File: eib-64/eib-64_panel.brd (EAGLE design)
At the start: 76.6 x 77.2 mm, 400 parts, among them J1 DF40-REC, J10 DF40-REC, J11 DF40-REC, J12 DF40-REC, J13 DF40-REC, J14 DF40-REC, J15 DF40-REC, J16 DF40-REC, J2 DF40-REC, J3 DF40-REC, J4 DF40-REC, J5 DF40-REC, J6 DF40-REC, J7 DF40-REC, J8 DF40-REC, J9 DF40-REC

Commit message: Updates to eib-64 for latest shuttle drives
- Decreased outer diameter
- Removed flat spots because they are not required anymore (headstage
retention clips were removed from drive body design)
- Remade panel and added labelled fiducial marks as per Filipe's
requirments
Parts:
- removed GND: LRG_GP, jonnew:GOLDPIN_0.5ID_0.7OD
- added E$1, E$2, E$4: (no value), fiducial:FIDUCIAL
- added GND31: LRG_GP, jonnew:GOLDPIN_0.5ID_0.7OD
- moved GND30 74.9 mm to (81.0, 97.6)
- moved GND28 72.5 mm to (61.0, 97.6)
- moved GND26 70.4 mm to (41.0, 97.6)
- moved GND24 68.6 mm to (21.0, 97.6)
- moved ESTIM15 64.1 mm to (87.4, 94.7)
- moved AN15 64.1 mm to (75.0, 95.4)
- moved CAT31 64.1 mm to (75.6, 94.7)
- moved J16 64.1 mm to (81.0, 92.0)
- moved REF15 64.1 mm to (86.5, 94.7)
- moved TET240 64.1 mm to (81.0, 91.0)
- moved TET241 64.1 mm to (81.0, 91.0)
- moved TET242 64.1 mm to (81.0, 91.0)
- moved TET243 64.1 mm to (81.0, 91.0)
- moved TET244 64.1 mm to (81.0, 91.0)
- moved TET245 64.1 mm to (81.0, 91.0)
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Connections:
- net GND: now also GND31.P$1; no longer GND.P$1
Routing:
- net GND: track 0.00 -> 40.6 mm, vias 240 -> 320
- net CAT7: track 6.44 -> 5.35 mm
- net CAT3: track 6.44 -> 5.35 mm
- net CAT19: track 6.44 -> 5.35 mm
- net CAT23: track 6.44 -> 5.35 mm
- net CAT15: track 6.44 -> 5.35 mm
- net CAT1: track 6.44 -> 5.35 mm
- net CAT11: track 6.44 -> 5.35 mm
- net CAT5: track 6.44 -> 5.35 mm
- net CAT17: track 6.44 -> 5.35 mm
- net CAT9: track 6.44 -> 5.35 mm
- net CAT31: track 6.44 -> 5.35 mm
- net CAT27: track 6.44 -> 5.35 mm
- net CAT21: track 6.44 -> 5.35 mm
- net CAT13: track 6.44 -> 5.35 mm
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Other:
- board size 76.6 x 77.2 mm -> 102 x 113 mm
- board text added: "(6, 11)"
- board text added: "(92, 97)"
- board text added: "(95, 20)"
- board text added: "CERN OHL v1.2 JPN, MWL@MIT 2019"
- board text added: "EIB-64 Rev. 1.2"
- board text added: "EIB-64 r1.2 JPN '19 OHL v1.2"
- board text added: "r1.2"
- board text removed: "EIB-64 JPN '17 OHL v1.2"
- board text removed: "EIB-64 r1.1"
- board text removed: "V-CUT"

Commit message: Address Filipe's issues with eib-64 prior to fabrication
- Move mouse bites on panel away from connector since it will be hard to
sand under there.
- Reduce ground planes around mouse bites to prvent exposued copper
after sanding.
- Adde "Open Ephys" to bottom silk.
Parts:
- removed GND31: LRG_GP, jonnew:GOLDPIN_0.5ID_0.7OD
- added GND: LRG_GP, jonnew:GOLDPIN_0.5ID_0.7OD
- moved GND15 72.7 mm to (14.4, 68.0), turned to 90 degrees
- moved GND23 72.7 mm to (14.4, 91.0), turned to 90 degrees
- moved GND7 72.7 mm to (14.4, 45.0), turned to 90 degrees
- moved GND13 14.7 mm to (74.4, 45.0), turned to 90 degrees
- moved GND21 14.7 mm to (74.4, 68.0), turned to 90 degrees
- moved GND5 14.7 mm to (74.4, 22.0), turned to 90 degrees
- moved GND29 14.7 mm to (74.4, 91.0), turned to 90 degrees
- moved GND1 14.7 mm to (34.4, 22.0), turned to 90 degrees
- moved GND11 14.7 mm to (54.4, 45.0), turned to 90 degrees
- moved GND17 14.7 mm to (34.4, 68.0), turned to 90 degrees
- moved GND19 14.7 mm to (54.4, 68.0), turned to 90 degrees
- moved GND3 14.7 mm to (54.4, 22.0), turned to 90 degrees
- moved GND9 14.7 mm to (34.4, 45.0), turned to 90 degrees
- moved GND25 14.7 mm to (34.4, 91.0), turned to 90 degrees
- moved GND27 14.7 mm to (54.4, 91.0), turned to 90 degrees
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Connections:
- new net GND1: GND1.P$1, GND2.P$1, J2.70, SHLD_A1.P$1
- new net GND10: GND19.P$1, GND20.P$1, J11.70, SHLD_A10.P$1
- new net GND11: GND21.P$1, GND22.P$1, J12.70, SHLD_A11.P$1
- new net GND12: GND23.P$1, GND24.P$1, J13.70, SHLD_A12.P$1
- new net GND13: GND25.P$1, GND26.P$1, J14.70, SHLD_A13.P$1
- new net GND14: GND27.P$1, GND28.P$1, J15.70, SHLD_A14.P$1
- new net GND15: GND29.P$1, GND30.P$1, J16.70, SHLD_A15.P$1
- new net GND2: GND3.P$1, GND4.P$1, J3.70, SHLD_A2.P$1
- new net GND3: GND5.P$1, GND6.P$1, J4.70, SHLD_A3.P$1
- new net GND4: GND7.P$1, GND8.P$1, J5.70, SHLD_A4.P$1
- new net GND5: GND10.P$1, GND9.P$1, J6.70, SHLD_A5.P$1
- new net GND6: GND11.P$1, GND12.P$1, J7.70, SHLD_A6.P$1
- new net GND7: GND13.P$1, GND14.P$1, J8.70, SHLD_A7.P$1
- new net GND8: GND15.P$1, GND16.P$1, J9.70, SHLD_A8.P$1
- new net GND9: GND17.P$1, GND18.P$1, J10.70, SHLD_A9.P$1
- net GND: now also GND.P$1; no longer GND1.P$1, GND10.P$1, GND11.P$1, GND12.P$1, GND13.P$1, GND14.P$1, GND15.P$1, GND16.P$1, GND17.P$1, GND18.P$1, GND19.P$1, GND2.P$1, GND20.P$1, GND21.P$1, GND22.P$1, GND23.P$1, GND24.P$1, GND25.P$1, GND26.P$1, GND27.P$1, GND28.P$1, GND29.P$1, GND3.P$1, GND30.P$1, GND31.P$1, GND4.P$1, GND5.P$1, GND6.P$1, GND7.P$1, GND8.P$1, GND9.P$1, J10.70, J11.70, J12.70, J13.70, J14.70, J15.70, J16.70, J2.70, J3.70, J4.70, J5.70, J6.70, J7.70, J8.70, J9.70, SHLD_A1.P$1, SHLD_A10.P$1, SHLD_A11.P$1, SHLD_A12.P$1, SHLD_A13.P$1, SHLD_A14.P$1, SHLD_A15.P$1, SHLD_A2.P$1, SHLD_A3.P$1, SHLD_A4.P$1, SHLD_A5.P$1, SHLD_A6.P$1, SHLD_A7.P$1, SHLD_A8.P$1, SHLD_A9.P$1
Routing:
- net GND: track 40.6 -> 2.54 mm, vias 320 -> 20
- net GND7: track 0.00 -> 2.54 mm, vias 0 -> 20
- net GND15: track 0.00 -> 2.54 mm, vias 0 -> 20
- net GND11: track 0.00 -> 2.54 mm, vias 0 -> 20
- net GND9: track 0.00 -> 2.54 mm, vias 0 -> 20
- net GND6: track 0.00 -> 2.54 mm, vias 0 -> 20
- net GND5: track 0.00 -> 2.54 mm, vias 0 -> 20
- net GND14: track 0.00 -> 2.54 mm, vias 0 -> 20
- net GND13: track 0.00 -> 2.54 mm, vias 0 -> 20
- net GND10: track 0.00 -> 2.54 mm, vias 0 -> 20
- net GND3: track 0.00 -> 2.54 mm, vias 0 -> 20
- net GND2: track 0.00 -> 2.54 mm, vias 0 -> 20
- net GND1: track 0.00 -> 2.54 mm, vias 0 -> 20
- net GND8: track 0.00 -> 2.54 mm, vias 0 -> 20
- net GND4: track 0.00 -> 2.54 mm, vias 0 -> 20
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- added copper zone on layer 1, net GND1
- added copper zone on layer 15, net GND1
- added copper zone on layer 16, net GND1
- added copper zone on layer 2, net GND1
- added copper zone on layer 1, net GND10
- added copper zone on layer 15, net GND10
- added copper zone on layer 16, net GND10
- added copper zone on layer 2, net GND10
- added copper zone on layer 1, net GND11
- added copper zone on layer 15, net GND11
- added copper zone on layer 16, net GND11
- added copper zone on layer 2, net GND11
- added copper zone on layer 1, net GND12
- added copper zone on layer 15, net GND12
- added copper zone on layer 16, net GND12
- added copper zone on layer 2, net GND12
- added copper zone on layer 1, net GND13
- added copper zone on layer 15, net GND13
- added copper zone on layer 16, net GND13
- added copper zone on layer 2, net GND13
- added copper zone on layer 1, net GND14
- added copper zone on layer 15, net GND14
- added copper zone on layer 16, net GND14
- added copper zone on layer 2, net GND14
- added copper zone on layer 1, net GND15
- added copper zone on layer 15, net GND15
- added copper zone on layer 16, net GND15
- added copper zone on layer 2, net GND15
- added copper zone on layer 1, net GND2
- added copper zone on layer 15, net GND2
- added copper zone on layer 16, net GND2
- added copper zone on layer 2, net GND2
- added copper zone on layer 1, net GND3
- added copper zone on layer 15, net GND3
- added copper zone on layer 16, net GND3
- added copper zone on layer 2, net GND3
- added copper zone on layer 1, net GND4
- added copper zone on layer 15, net GND4
- added copper zone on layer 16, net GND4
- added copper zone on layer 2, net GND4
- added copper zone on layer 1, net GND5
- added copper zone on layer 15, net GND5
- added copper zone on layer 16, net GND5
- added copper zone on layer 2, net GND5
- added copper zone on layer 1, net GND6
- added copper zone on layer 15, net GND6
- added copper zone on layer 16, net GND6
- added copper zone on layer 2, net GND6
- added copper zone on layer 1, net GND7
- added copper zone on layer 15, net GND7
- added copper zone on layer 16, net GND7
- added copper zone on layer 2, net GND7
- added copper zone on layer 1, net GND8
- added copper zone on layer 15, net GND8
- added copper zone on layer 16, net GND8
- added copper zone on layer 2, net GND8
- added copper zone on layer 1, net GND9
- added copper zone on layer 15, net GND9
- added copper zone on layer 16, net GND9
- added copper zone on layer 2, net GND9
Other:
- board text added: "(94, 20)"
- board text added: "CERN OHL v1.2 JPN & Open Ephys Created in MWL@MIT 2019"
- board text added: "EIB-64, r1.2 JPN & Open Ephys OHL v1.2 '19"
- board text added: "Open Ephys EIB-64 Rev. 1.2"
- board text removed: "(95, 20)"
- board text removed: "CERN OHL v1.2 JPN, MWL@MIT 2019"
- board text removed: "EIB-64 Rev. 1.2"
- board text removed: "EIB-64 r1.2 JPN '19 OHL v1.2"

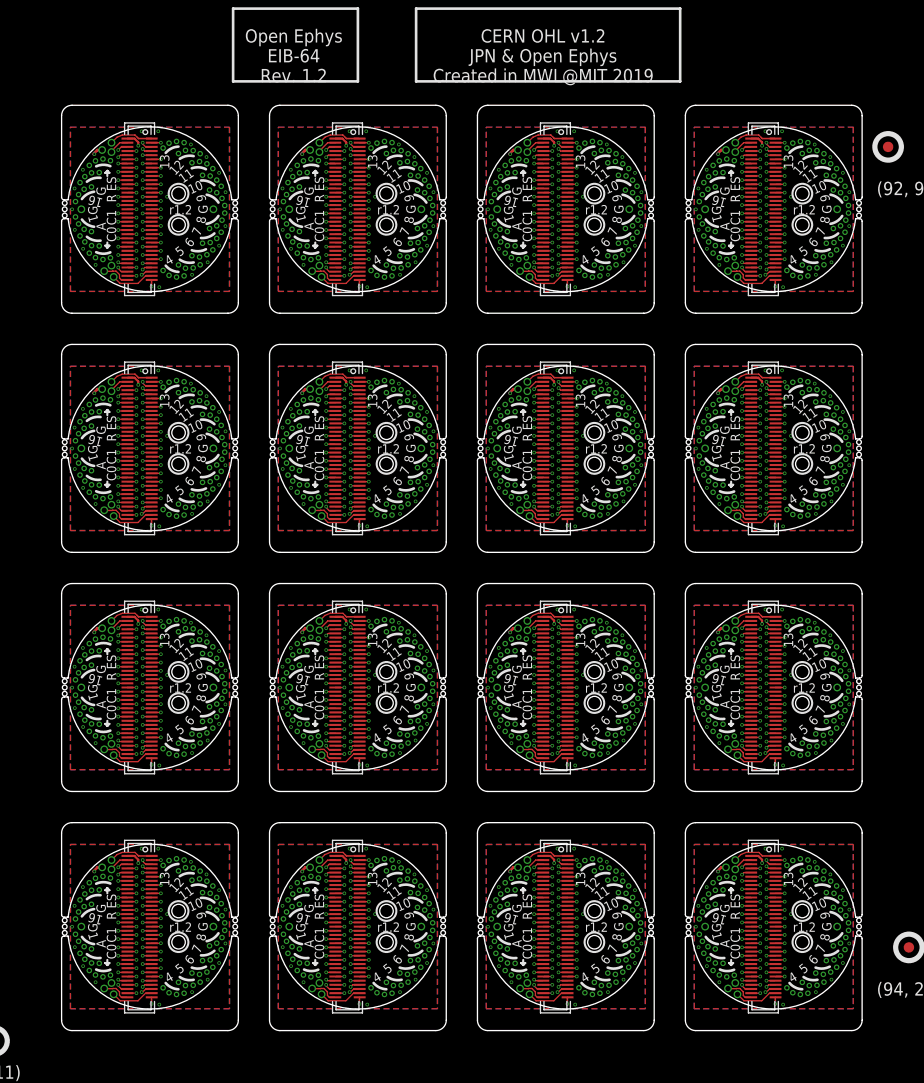
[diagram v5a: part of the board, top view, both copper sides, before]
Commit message: headstage-64 rev. 1.4 along with all dependencies
- This is headstage-64 revision 1.4. Because it involves a change in the
bottom analog connector, a lot of other boards had to be changed to
match the new pinout. That is why there are so many files in this
commit. Changes in revision 1.4 and affects on other boards are as
follows:

1. The coaxial adapter board has been improved to allow a regulator to
sit on the daughter board. To do this, the filtered vcoax had to brought
back to the daughter board and then out again after regulation. Of
course this regulation can be bypassed simply by connecting these
contacts

2. Vcoax decoupling has been greatly improved to lower impedance of
power input. There is now 70 uF of decoupling capacitance on the
post-regulated vcoax.

3. The JTAG interface was changed to allow it to be enabled and disabled
by the programmer. This means that these pins are nominally used for
extra IO. The programmer now contains a jumper that allows it operate in
this new mode (closed) or legacy mode (open) for headstage-64 rev 1.3.

4. All of the serializers GPIO lines are now all routed to the FPGA.

5. The opto and estim circuits no longer share SPI lines so they can be
operated independently.

6. The analog routing to the intan chip has been changed such that the
electrode lines are shielded from vcoax, which was polluting the anlog
signals, by a ground pin. This means that eibs etc. need to respect this
new pinout. This is why eib-64, eib-64-large, nanoz-adapter,
omnetics-adapter-64, and test-board-64 have been changed.

7. The serializer on headstage-64 has been upgraded to DS90UB933-Q1
which has reduced back channel latencies, increased forward channel
bandwidth, and improved performance with
imperfect cabling.

8. There is a solder jumper on the bottom of headstage-64 to allow the
addition of an external resistor to AUXIN3 on the intan to allow it to
operate at lower bandwidths. This comes at the cost of not being able to
measure istim unless t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
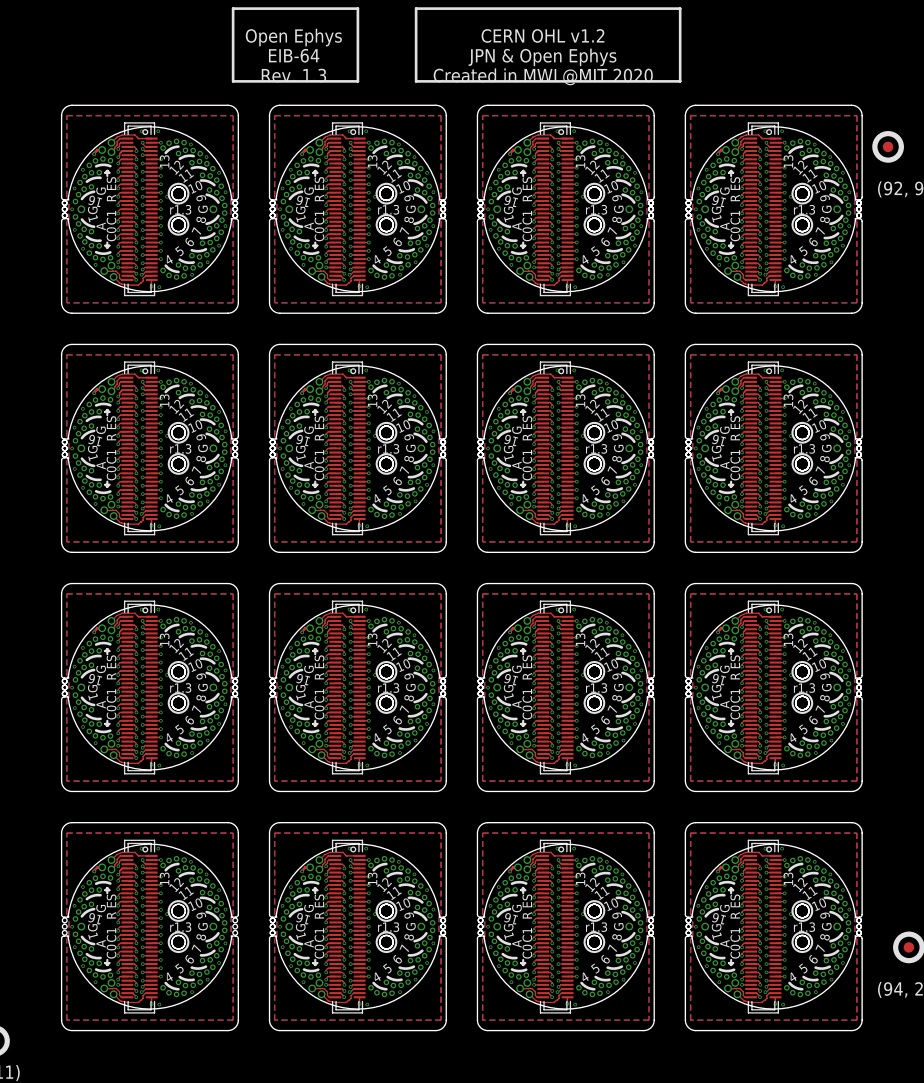
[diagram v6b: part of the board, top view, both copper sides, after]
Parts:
- removed GND: LRG_GP, jonnew:GOLDPIN_0.5ID_0.7OD
- added GND31: LRG_GP, jonnew:GOLDPIN_0.5ID_0.7OD
- moved GND15 76.3 mm to (87.1, 45.0)
- moved GND23 76.3 mm to (87.1, 68.0)
- moved GND7 76.3 mm to (87.1, 22.0)
- moved GND10 12.7 mm to (34.4, 45.0)
- moved GND18 12.7 mm to (34.4, 68.0)
- moved GND2 12.7 mm to (34.4, 22.0)
- moved GND26 12.7 mm to (34.4, 91.0)
- moved GND16 12.7 mm to (14.4, 68.0)
- moved GND24 12.7 mm to (14.4, 91.0)
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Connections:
- net GND: now also GND1.P$1, J1.37; no longer GND.P$1, J1.70
- net GND1: now also GND3.P$1, J2.37; no longer GND1.P$1, J2.70
- net GND10: now also GND21.P$1, J11.37; no longer GND19.P$1, J11.70
- net GND11: now also GND23.P$1, J12.37; no longer GND21.P$1, J12.70
- net GND12: now also GND25.P$1, J13.37; no longer GND23.P$1, J13.70
- net GND13: now also GND27.P$1, J14.37; no longer GND25.P$1, J14.70
- net GND14: now also GND29.P$1, J15.37; no longer GND27.P$1, J15.70
- net GND15: now also GND31.P$1, J16.37; no longer GND29.P$1, J16.70
- net GND2: now also GND5.P$1, J3.37; no longer GND3.P$1, J3.70
- net GND3: now also GND7.P$1, J4.37; no longer GND5.P$1, J4.70
- net GND4: now also GND9.P$1, J5.37; no longer GND7.P$1, J5.70
- net GND5: now also GND11.P$1, J6.37; no longer GND9.P$1, J6.70
- net GND6: now also GND13.P$1, J7.37; no longer GND11.P$1, J7.70
- net GND7: now also GND15.P$1, J8.37; no longer GND13.P$1, J8.70
- net GND8: now also GND17.P$1, J9.37; no longer GND15.P$1, J9.70
- net GND9: now also GND19.P$1, J10.37; no longer GND17.P$1, J10.70
- net N$1: now also J1.69; no longer J1.68
- net N$10: now also J1.60; no longer J1.59
- net N$100: now also J2.38; no longer J2.37
- net N$1000: now also J16.56; no longer J16.55
- net N$1001: now also J16.55; no longer J16.54
- net N$1002: now also J16.54; no longer J16.53
- net N$1003: now also J16.53; no longer J16.52
- net N$1004: now also J16.52; no longer J16.51
- net N$1005: now also J16.51; no longer J16.50
- net N$1006: now also J16.50; no longer J16.49
- net N$1007: now also J16.49; no longer J16.48
- net N$1008: now also J16.48; no longer J16.47
- net N$1009: now also J16.47; no longer J16.46
- net N$1010: now also J16.46; no longer J16.45
- net N$1011: now also J16.45; no longer J16.44
- net N$1012: now also J16.44; no longer J16.43
- net N$1013: now also J16.43; no longer J16.42
- net N$1014: now also J16.42; no longer J16.41
- net N$1015: now also J16.41; no longer J16.40
- net N$1016: now also J16.39; no longer J16.38
- net N$1021: now also J16.66; no longer J16.65
- net N$1022: now also J16.68; no longer J16.67
- net N$1023: now also J16.40; no longer J16.39
- net N$1024: now also J16.38; no longer J16.37
- net N$11: now also J1.59; no longer J1.58
- net N$12: now also J1.58; no longer J1.57
- net N$129: now also J3.69; no longer J3.68
- net N$13: now also J1.57; no longer J1.56
- net N$130: now also J3.67; no longer J3.66
- net N$131: now also J3.65; no longer J3.64
- net N$132: now also J3.64; no longer J3.63
- net N$133: now also J3.63; no longer J3.62
- net N$134: now also J3.62; no longer J3.61
- net N$135: now also J3.61; no longer J3.60
- net N$136: now also J3.60; no longer J3.59
- net N$137: now also J3.59; no longer J3.58
- net N$138: now also J3.58; no longer J3.57
- net N$139: now also J3.57; no longer J3.56
- net N$14: now also J1.56; no longer J1.55
- net N$140: now also J3.56; no longer J3.55
- net N$141: now also J3.55; no longer J3.54
- net N$142: now also J3.54; no longer J3.53
- net N$143: now also J3.53; no longer J3.52
- net N$144: now also J3.52; no longer J3.51
- net N$145: now also J3.51; no longer J3.50
- net N$146: now also J3.50; no longer J3.49
- net N$147: now also J3.49; no longer J3.48
- net N$148: now also J3.48; no longer J3.47
- net N$149: now also J3.47; no longer J3.46
- net N$15: now also J1.55; no longer J1.54
- net N$150: now also J3.46; no longer J3.45
- net N$151: now also J3.45; no longer J3.44
- net N$152: now also J3.44; no longer J3.43
- net N$153: now also J3.43; no longer J3.42
- net N$154: now also J3.42; no longer J3.41
- net N$155: now also J3.41; no longer J3.40
- net N$156: now also J3.39; no longer J3.38
- net N$16: now also J1.54; no longer J1.53
- net N$161: now also J3.66; no longer J3.65
- net N$162: now also J3.68; no longer J3.67
- net N$163: now also J3.40; no longer J3.39
- net N$164: now also J3.38; no longer J3.37
- net N$17: now also J1.53; no longer J1.52
- net N$18: now also J1.52; no longer J1.51
- net N$19: now also J1.51; no longer J1.50
- net N$193: now also J4.69; no longer J4.68
- net N$194: now also J4.67; no longer J4.66
- net N$195: now also J4.65; no longer J4.64
- net N$196: now also J4.64; no longer J4.63
- net N$197: now also J4.63; no longer J4.62
- net N$198: now also J4.62; no longer J4.61
- net N$2: now also J1.66; no longer J1.65
- net N$20: now also J1.50; no longer J1.49
- net N$21: now also J1.49; no longer J1.48
- net N$22: now also J1.48; no longer J1.47
- net N$227: now also J4.61; no longer J4.60
- net N$228: now also J4.60; no longer J4.59
- net N$229: now also J4.59; no longer J4.58
- net N$23: now also J1.47; no longer J1.46
- net N$230: now also J4.58; no longer J4.57
- net N$231: now also J4.57; no longer J4.56
- net N$232: now also J4.56; no longer J4.55
- net N$233: now also J4.55; no longer J4.54
- net N$234: now also J4.54; no longer J4.53
- net N$235: now also J4.53; no longer J4.52
- net N$236: now also J4.52; no longer J4.51
- net N$237: now also J4.51; no longer J4.50
- net N$238: now also J4.50; no longer J4.49
- net N$239: now also J4.49; no longer J4.48
- net N$24: now also J1.46; no longer J1.45
- net N$240: now also J4.48; no longer J4.47
- net N$241: now also J4.47; no longer J4.46
- net N$242: now also J4.46; no longer J4.45
- net N$243: now also J4.45; no longer J4.44
- net N$244: now also J4.44; no longer J4.43
- net N$245: now also J4.43; no longer J4.42
- net N$246: now also J4.42; no longer J4.41
- net N$247: now also J4.41; no longer J4.40
- net N$248: now also J4.39; no longer J4.38
- net N$25: now also J1.45; no longer J1.44
- net N$253: now also J4.66; no longer J4.65
- net N$254: now also J4.68; no longer J4.67
- net N$255: now also J4.40; no longer J4.39
- net N$256: now also J4.38; no longer J4.37
- net N$26: now also J1.44; no longer J1.43
- net N$27: now also J1.43; no longer J1.42
- net N$28: now also J1.42; no longer J1.41
- net N$285: now also J5.69; no longer J5.68
- net N$286: now also J5.67; no longer J5.66
- net N$287: now also J5.65; no longer J5.64
- net N$288: now also J5.64; no longer J5.63
- net N$289: now also J5.63; no longer J5.62
- net N$29: now also J1.41; no longer J1.40
- net N$290: now also J5.62; no longer J5.61
- net N$291: now also J5.61; no longer J5.60
- net N$292: now also J5.60; no longer J5.59
- net N$293: now also J5.59; no longer J5.58
- net N$294: now also J5.58; no longer J5.57
- net N$295: now also J5.57; no longer J5.56
- net N$296: now also J5.56; no longer J5.55
- net N$297: now also J5.55; no longer J5.54
- net N$298: now also J5.54; no longer J5.53
- net N$299: now also J5.53; no longer J5.52
- net N$3: now also J1.67; no longer J1.66
- net N$30: now also J1.40; no longer J1.39
- net N$300: now also J5.52; no longer J5.51
- net N$301: now also J5.51; no longer J5.50
- net N$302: now also J5.50; no longer J5.49
- net N$303: now also J5.49; no longer J5.48
- net N$304: now also J5.48; no longer J5.47
- net N$305: now also J5.47; no longer J5.46
- net N$306: now also J5.46; no longer J5.45
- net N$307: now also J5.45; no longer J5.44
- net N$308: now also J5.44; no longer J5.43
- net N$309: now also J5.43; no longer J5.42
- net N$31: now also J1.39; no longer J1.38
- net N$310: now also J5.42; no longer J5.41
- net N$311: now also J5.41; no longer J5.40
- net N$312: now also J5.39; no longer J5.38
- net N$317: now also J5.66; no longer J5.65
- net N$318: now also J5.68; no longer J5.67
- net N$319: now also J5.40; no longer J5.39
- net N$32: now also J1.38; no longer J1.37
- net N$320: now also J5.38; no longer J5.37
- net N$349: now also J6.69; no longer J6.68
- net N$350: now also J6.67; no longer J6.66
- net N$351: now also J6.65; no longer J6.64
- net N$352: now also J6.64; no longer J6.63
- net N$353: now also J6.63; no longer J6.62
- net N$354: now also J6.62; no longer J6.61
- net N$355: now also J6.61; no longer J6.60
- net N$356: now also J6.60; no longer J6.59
- net N$357: now also J6.59; no longer J6.58
- net N$358: now also J6.58; no longer J6.57
- net N$359: now also J6.57; no longer J6.56
- net N$360: now also J6.56; no longer J6.55
- net N$361: now also J6.55; no longer J6.54
- net N$362: now also J6.54; no longer J6.53
- net N$363: now also J6.53; no longer J6.52
- net N$364: now also J6.52; no longer J6.51
- net N$365: now also J6.51; no longer J6.50
- net N$366: now also J6.50; no longer J6.49
- net N$367: now also J6.49; no longer J6.48
- net N$368: now also J6.48; no longer J6.47
- net N$369: now also J6.47; no longer J6.46
- net N$370: now also J6.46; no longer J6.45
- net N$371: now also J6.45; no longer J6.44
- net N$372: now also J6.44; no longer J6.43
- net N$373: now also J6.43; no longer J6.42
- net N$374: now also J6.42; no longer J6.41
- net N$375: now also J6.41; no longer J6.40
- net N$376: now also J6.39; no longer J6.38
- net N$381: now also J6.66; no longer J6.65
- net N$382: now also J6.68; no longer J6.67
- net N$383: now also J6.40; no longer J6.39
- net N$384: now also J6.38; no longer J6.37
- net N$4: now also J1.68; no longer J1.67
- net N$413: now also J7.69; no longer J7.68
- net N$414: now also J7.67; no longer J7.66
- net N$415: now also J7.65; no longer J7.64
- net N$416: now also J7.64; no longer J7.63
- net N$417: now also J7.63; no longer J7.62
- net N$418: now also J7.62; no longer J7.61
- net N$419: now also J7.61; no longer J7.60
- net N$420: now also J7.60; no longer J7.59
- net N$421: now also J7.59; no longer J7.58
- net N$422: now also J7.58; no longer J7.57
- net N$423: now also J7.57; no longer J7.56
- net N$424: now also J7.56; no longer J7.55
- net N$425: now also J7.55; no longer J7.54
- net N$426: now also J7.54; no longer J7.53
- net N$427: now also J7.53; no longer J7.52
- net N$428: now also J7.52; no longer J7.51
- net N$429: now also J7.51; no longer J7.50
- net N$430: now also J7.50; no longer J7.49
- net N$431: now also J7.49; no longer J7.48
- net N$432: now also J7.48; no longer J7.47
- net N$433: now also J7.47; no longer J7.46
- net N$434: now also J7.46; no longer J7.45
- net N$435: now also J7.45; no longer J7.44
- net N$436: now also J7.44; no longer J7.43
- net N$437: now also J7.43; no longer J7.42
- net N$438: now also J7.42; no longer J7.41
- net N$439: now also J7.41; no longer J7.40
- net N$440: now also J7.39; no longer J7.38
- net N$445: now also J7.66; no longer J7.65
- net N$446: now also J7.68; no longer J7.67
- net N$447: now also J7.40; no longer J7.39
- net N$448: now also J7.38; no longer J7.37
- net N$477: now also J8.69; no longer J8.68
- net N$478: now also J8.67; no longer J8.66
- net N$479: now also J8.65; no longer J8.64
- net N$480: now also J8.64; no longer J8.63
- net N$481: now also J8.63; no longer J8.62
- net N$482: now also J8.62; no longer J8.61
- net N$483: now also J8.61; no longer J8.60
- net N$484: now also J8.60; no longer J8.59
- net N$485: now also J8.59; no longer J8.58
- net N$486: now also J8.58; no longer J8.57
- net N$487: now also J8.57; no longer J8.56
- net N$488: now also J8.56; no longer J8.55
- net N$489: now also J8.55; no longer J8.54
- net N$490: now also J8.54; no longer J8.53
- net N$491: now also J8.53; no longer J8.52
- net N$492: now also J8.52; no longer J8.51
- net N$493: now also J8.51; no longer J8.50
- net N$494: now also J8.50; no longer J8.49
- net N$495: now also J8.49; no longer J8.48
- net N$496: now also J8.48; no longer J8.47
- net N$497: now also J8.47; no longer J8.46
- net N$498: now also J8.46; no longer J8.45
- net N$499: now also J8.45; no longer J8.44
- net N$5: now also J1.65; no longer J1.64
- net N$500: now also J8.44; no longer J8.43
- net N$501: now also J8.43; no longer J8.42
- net N$502: now also J8.42; no longer J8.41
- net N$503: now also J8.41; no longer J8.40
- net N$504: now also J8.39; no longer J8.38
- net N$509: now also J8.66; no longer J8.65
- net N$510: now also J8.68; no longer J8.67
- net N$511: now also J8.40; no longer J8.39
- net N$512: now also J8.38; no longer J8.37
- net N$541: now also J9.69; no longer J9.68
- net N$542: now also J9.67; no longer J9.66
- net N$543: now also J9.65; no longer J9.64
- net N$544: now also J9.64; no longer J9.63
- net N$545: now also J9.63; no longer J9.62
- net N$546: now also J9.62; no longer J9.61
- net N$547: now also J9.61; no longer J9.60
- net N$548: now also J9.60; no longer J9.59
- net N$549: now also J9.59; no longer J9.58
- net N$550: now also J9.58; no longer J9.57
- net N$551: now also J9.57; no longer J9.56
- net N$552: now also J9.56; no longer J9.55
- net N$553: now also J9.55; no longer J9.54
- net N$554: now also J9.54; no longer J9.53
- net N$555: now also J9.53; no longer J9.52
- net N$556: now also J9.52; no longer J9.51
- net N$557: now also J9.51; no longer J9.50
- net N$558: now also J9.50; no longer J9.49
- net N$559: now also J9.49; no longer J9.48
- net N$560: now also J9.48; no longer J9.47
- net N$561: now also J9.47; no longer J9.46
- net N$562: now also J9.46; no longer J9.45
- net N$563: now also J9.45; no longer J9.44
- net N$564: now also J9.44; no longer J9.43
- net N$565: now also J9.43; no longer J9.42
- net N$566: now also J9.42; no longer J9.41
- net N$567: now also J9.41; no longer J9.40
- net N$568: now also J9.39; no longer J9.38
- net N$573: now also J9.66; no longer J9.65
- net N$574: now also J9.68; no longer J9.67
- net N$575: now also J9.40; no longer J9.39
- net N$576: now also J9.38; no longer J9.37
- net N$6: now also J1.64; no longer J1.63
- net N$605: now also J10.69; no longer J10.68
- net N$606: now also J10.67; no longer J10.66
- net N$607: now also J10.65; no longer J10.64
- net N$608: now also J10.64; no longer J10.63
- net N$609: now also J10.63; no longer J10.62
- net N$610: now also J10.62; no longer J10.61
- net N$611: now also J10.61; no longer J10.60
- net N$612: now also J10.60; no longer J10.59
- net N$613: now also J10.59; no longer J10.58
- net N$614: now also J10.58; no longer J10.57
- net N$615: now also J10.57; no longer J10.56
- net N$616: now also J10.56; no longer J10.55
- net N$617: now also J10.55; no longer J10.54
- net N$618: now also J10.54; no longer J10.53
- net N$619: now also J10.53; no longer J10.52
- net N$620: now also J10.52; no longer J10.51
- net N$621: now also J10.51; no longer J10.50
- net N$622: now also J10.50; no longer J10.49
- net N$623: now also J10.49; no longer J10.48
- net N$624: now also J10.48; no longer J10.47
- net N$625: now also J10.47; no longer J10.46
- net N$626: now also J10.46; no longer J10.45
- net N$627: now also J10.45; no longer J10.44
- net N$628: now also J10.44; no longer J10.43
- net N$629: now also J10.43; no longer J10.42
- net N$630: now also J10.42; no longer J10.41
- net N$631: now also J10.41; no longer J10.40
- net N$632: now also J10.39; no longer J10.38
- net N$637: now also J10.66; no longer J10.65
- net N$638: now also J10.68; no longer J10.67
- net N$639: now also J10.40; no longer J10.39
- net N$640: now also J10.38; no longer J10.37
- net N$65: now also J2.69; no longer J2.68
- net N$66: now also J2.67; no longer J2.66
- net N$669: now also J11.69; no longer J11.68
- net N$67: now also J2.65; no longer J2.64
- net N$670: now also J11.67; no longer J11.66
- net N$671: now also J11.65; no longer J11.64
- net N$672: now also J11.64; no longer J11.63
- net N$673: now also J11.63; no longer J11.62
- net N$674: now also J11.62; no longer J11.61
- net N$675: now also J11.61; no longer J11.60
- net N$676: now also J11.60; no longer J11.59
- net N$677: now also J11.59; no longer J11.58
- net N$678: now also J11.58; no longer J11.57
- net N$679: now also J11.57; no longer J11.56
- net N$68: now also J2.64; no longer J2.63
- net N$680: now also J11.56; no longer J11.55
- net N$681: now also J11.55; no longer J11.54
- net N$682: now also J11.54; no longer J11.53
- net N$683: now also J11.53; no longer J11.52
- net N$684: now also J11.52; no longer J11.51
- net N$685: now also J11.51; no longer J11.50
- net N$686: now also J11.50; no longer J11.49
- net N$687: now also J11.49; no longer J11.48
- net N$688: now also J11.48; no longer J11.47
- net N$689: now also J11.47; no longer J11.46
- net N$69: now also J2.63; no longer J2.62
- net N$690: now also J11.46; no longer J11.45
- net N$691: now also J11.45; no longer J11.44
- net N$692: now also J11.44; no longer J11.43
- net N$693: now also J11.43; no longer J11.42
- net N$694: now also J11.42; no longer J11.41
- net N$695: now also J11.41; no longer J11.40
- net N$696: now also J11.39; no longer J11.38
- net N$7: now also J1.63; no longer J1.62
- net N$70: now also J2.62; no longer J2.61
- net N$701: now also J11.66; no longer J11.65
- net N$702: now also J11.68; no longer J11.67
- net N$703: now also J11.40; no longer J11.39
- net N$704: now also J11.38; no longer J11.37
- net N$71: now also J2.61; no longer J2.60
- net N$72: now also J2.60; no longer J2.59
- net N$73: now also J2.59; no longer J2.58
- net N$733: now also J12.69; no longer J12.68
- net N$734: now also J12.67; no longer J12.66
- net N$735: now also J12.65; no longer J12.64
- net N$736: now also J12.64; no longer J12.63
- net N$737: now also J12.63; no longer J12.62
- net N$738: now also J12.62; no longer J12.61
- net N$739: now also J12.61; no longer J12.60
- net N$74: now also J2.58; no longer J2.57
- net N$740: now also J12.60; no longer J12.59
- net N$741: now also J12.59; no longer J12.58
- net N$742: now also J12.58; no longer J12.57
- net N$743: now also J12.57; no longer J12.56
- net N$744: now also J12.56; no longer J12.55
- net N$745: now also J12.55; no longer J12.54
- net N$746: now also J12.54; no longer J12.53
- net N$747: now also J12.53; no longer J12.52
- net N$748: now also J12.52; no longer J12.51
- net N$749: now also J12.51; no longer J12.50
- net N$75: now also J2.57; no longer J2.56
- net N$750: now also J12.50; no longer J12.49
- net N$751: now also J12.49; no longer J12.48
- net N$752: now also J12.48; no longer J12.47
- net N$753: now also J12.47; no longer J12.46
- net N$754: now also J12.46; no longer J12.45
- net N$755: now also J12.45; no longer J12.44
- net N$756: now also J12.44; no longer J12.43
- net N$757: now also J12.43; no longer J12.42
- net N$758: now also J12.42; no longer J12.41
- net N$759: now also J12.41; no longer J12.40
- net N$76: now also J2.56; no longer J2.55
- net N$760: now also J12.39; no longer J12.38
- net N$765: now also J12.66; no longer J12.65
- net N$766: now also J12.68; no longer J12.67
- net N$767: now also J12.40; no longer J12.39
- net N$768: now also J12.38; no longer J12.37
- net N$77: now also J2.55; no longer J2.54
- net N$78: now also J2.54; no longer J2.53
- net N$79: now also J2.53; no longer J2.52
- net N$797: now also J13.69; no longer J13.68
- net N$798: now also J13.67; no longer J13.66
- net N$799: now also J13.65; no longer J13.64
- net N$8: now also J1.62; no longer J1.61
- net N$80: now also J2.52; no longer J2.51
- net N$800: now also J13.64; no longer J13.63
- net N$801: now also J13.63; no longer J13.62
- net N$802: now also J13.62; no longer J13.61
- net N$803: now also J13.61; no longer J13.60
- net N$804: now also J13.60; no longer J13.59
- net N$805: now also J13.59; no longer J13.58
- net N$806: now also J13.58; no longer J13.57
- net N$807: now also J13.57; no longer J13.56
- net N$808: now also J13.56; no longer J13.55
- net N$809: now also J13.55; no longer J13.54
- net N$81: now also J2.51; no longer J2.50
- net N$810: now also J13.54; no longer J13.53
- net N$811: now also J13.53; no longer J13.52
- net N$812: now also J13.52; no longer J13.51
- net N$813: now also J13.51; no longer J13.50
- net N$814: now also J13.50; no longer J13.49
- net N$815: now also J13.49; no longer J13.48
- net N$816: now also J13.48; no longer J13.47
- net N$817: now also J13.47; no longer J13.46
- net N$818: now also J13.46; no longer J13.45
- net N$819: now also J13.45; no longer J13.44
- net N$82: now also J2.50; no longer J2.49
- net N$820: now also J13.44; no longer J13.43
- net N$821: now also J13.43; no longer J13.42
- net N$822: now also J13.42; no longer J13.41
- net N$823: now also J13.41; no longer J13.40
- net N$824: now also J13.39; no longer J13.38
- net N$829: now also J13.66; no longer J13.65
- net N$83: now also J2.49; no longer J2.48
- net N$830: now also J13.68; no longer J13.67
- net N$831: now also J13.40; no longer J13.39
- net N$832: now also J13.38; no longer J13.37
- net N$84: now also J2.48; no longer J2.47
- net N$85: now also J2.47; no longer J2.46
- net N$86: now also J2.46; no longer J2.45
- net N$861: now also J14.69; no longer J14.68
- net N$862: now also J14.67; no longer J14.66
- net N$863: now also J14.65; no longer J14.64
- net N$864: now also J14.64; no longer J14.63
- net N$865: now also J14.63; no longer J14.62
- net N$866: now also J14.62; no longer J14.61
- net N$867: now also J14.61; no longer J14.60
- net N$868: now also J14.60; no longer J14.59
- net N$869: now also J14.59; no longer J14.58
- net N$87: now also J2.45; no longer J2.44
- net N$870: now also J14.58; no longer J14.57
- net N$871: now also J14.57; no longer J14.56
- net N$872: now also J14.56; no longer J14.55
- net N$873: now also J14.55; no longer J14.54
- net N$874: now also J14.54; no longer J14.53
- net N$875: now also J14.53; no longer J14.52
- net N$876: now also J14.52; no longer J14.51
- net N$877: now also J14.51; no longer J14.50
- net N$878: now also J14.50; no longer J14.49
- net N$879: now also J14.49; no longer J14.48
- net N$88: now also J2.44; no longer J2.43
- net N$880: now also J14.48; no longer J14.47
- net N$881: now also J14.47; no longer J14.46
- net N$882: now also J14.46; no longer J14.45
- net N$883: now also J14.45; no longer J14.44
- net N$884: now also J14.44; no longer J14.43
- net N$885: now also J14.43; no longer J14.42
- net N$886: now also J14.42; no longer J14.41
- net N$887: now also J14.41; no longer J14.40
- net N$888: now also J14.39; no longer J14.38
- net N$89: now also J2.43; no longer J2.42
- net N$893: now also J14.66; no longer J14.65
- net N$894: now also J14.68; no longer J14.67
- net N$895: now also J14.40; no longer J14.39
- net N$896: now also J14.38; no longer J14.37
- net N$9: now also J1.61; no longer J1.60
- net N$90: now also J2.42; no longer J2.41
- net N$91: now also J2.41; no longer J2.40
- net N$92: now also J2.39; no longer J2.38
- net N$925: now also J15.69; no longer J15.68
- net N$926: now also J15.67; no longer J15.66
- net N$927: now also J15.65; no longer J15.64
- net N$928: now also J15.64; no longer J15.63
- net N$929: now also J15.63; no longer J15.62
- net N$930: now also J15.62; no longer J15.61
- net N$931: now also J15.61; no longer J15.60
- net N$932: now also J15.60; no longer J15.59
- net N$933: now also J15.59; no longer J15.58
- net N$934: now also J15.58; no longer J15.57
- net N$935: now also J15.57; no longer J15.56
- net N$936: now also J15.56; no longer J15.55
- net N$937: now also J15.55; no longer J15.54
- net N$938: now also J15.54; no longer J15.53
- net N$939: now also J15.53; no longer J15.52
- net N$940: now also J15.52; no longer J15.51
- net N$941: now also J15.51; no longer J15.50
- net N$942: now also J15.50; no longer J15.49
- net N$943: now also J15.49; no longer J15.48
- net N$944: now also J15.48; no longer J15.47
- net N$945: now also J15.47; no longer J15.46
- net N$946: now also J15.46; no longer J15.45
- net N$947: now also J15.45; no longer J15.44
- net N$948: now also J15.44; no longer J15.43
- net N$949: now also J15.43; no longer J15.42
- net N$950: now also J15.42; no longer J15.41
- net N$951: now also J15.41; no longer J15.40
- net N$952: now also J15.39; no longer J15.38
- net N$957: now also J15.66; no longer J15.65
- net N$958: now also J15.68; no longer J15.67
- net N$959: now also J15.40; no longer J15.39
- net N$960: now also J15.38; no longer J15.37
- net N$97: now also J2.66; no longer J2.65
- net N$98: now also J2.68; no longer J2.67
- net N$989: now also J16.69; no longer J16.68
- net N$99: now also J2.40; no longer J2.39
- net N$990: now also J16.67; no longer J16.66
- net N$991: now also J16.65; no longer J16.64
- net N$992: now also J16.64; no longer J16.63
- net N$993: now also J16.63; no longer J16.62
- net N$994: now also J16.62; no longer J16.61
- net N$995: now also J16.61; no longer J16.60
- net N$996: now also J16.60; no longer J16.59
- net N$997: now also J16.59; no longer J16.58
- net N$998: now also J16.58; no longer J16.57
- net N$999: now also J16.57; no longer J16.56
- net REF: now also J1.70; no longer J1.69
- net REF1: now also J2.70; no longer J2.69
- net REF10: now also J11.70; no longer J11.69
- net REF11: now also J12.70; no longer J12.69
- net REF12: now also J13.70; no longer J13.69
- net REF13: now also J14.70; no longer J14.69
- net REF14: now also J15.70; no longer J15.69
- net REF15: now also J16.70; no longer J16.69
- net REF2: now also J3.70; no longer J3.69
- net REF3: now also J4.70; no longer J4.69
- net REF4: now also J5.70; no longer J5.69
- net REF5: now also J6.70; no longer J6.69
- net REF6: now also J7.70; no longer J7.69
- net REF7: now also J8.70; no longer J8.69
- net REF8: now also J9.70; no longer J9.69
- net REF9: now also J10.70; no longer J10.69
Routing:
- net N$567: track 6.40 -> 7.07 mm
- net N$311: track 6.40 -> 7.07 mm
- net N$695: track 6.40 -> 7.07 mm
- net N$631: track 6.40 -> 7.07 mm
- net N$439: track 6.40 -> 7.07 mm
- net N$375: track 6.40 -> 7.07 mm
- net N$29: track 6.40 -> 7.07 mm
- net N$91: track 6.40 -> 7.07 mm
- net N$823: track 6.40 -> 7.07 mm
- net N$155: track 6.40 -> 7.07 mm
- net N$951: track 6.40 -> 7.07 mm
- net N$887: track 6.40 -> 7.07 mm
- net N$759: track 6.40 -> 7.07 mm
- net N$503: track 6.40 -> 7.07 mm
- net N$247: track 6.40 -> 7.07 mm
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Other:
- board text added: "CERN OHL v1.2 JPN & Open Ephys Created in MWL@MIT 2020"
- board text added: "Open Ephys EIB-64 Rev. 1.3"
- board text added: "r1.3"
- board text removed: "CERN OHL v1.2 JPN & Open Ephys Created in MWL@MIT 2019"
- board text removed: "Open Ephys EIB-64 Rev. 1.2"
- board text removed: "r1.2"
